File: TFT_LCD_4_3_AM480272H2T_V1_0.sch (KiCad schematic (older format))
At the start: 1 part, among them P1 HRS_FH28

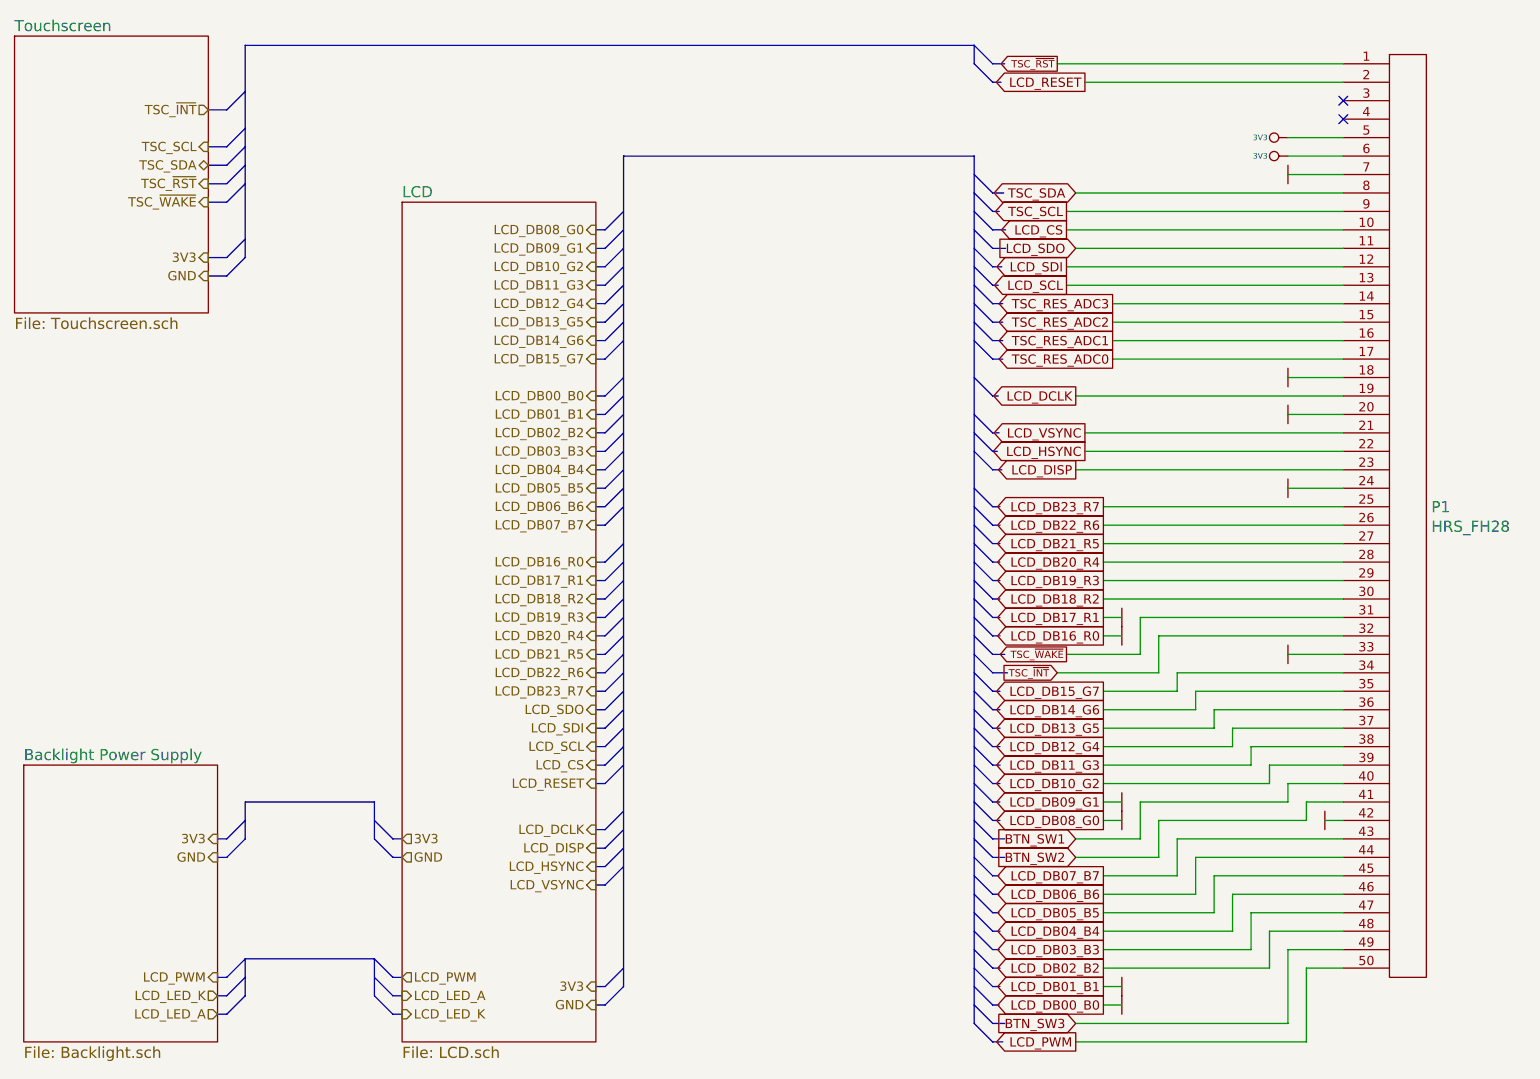
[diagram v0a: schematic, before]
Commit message: Schematic finished, needes to be rechecked, pcb finished needes to be tweeked
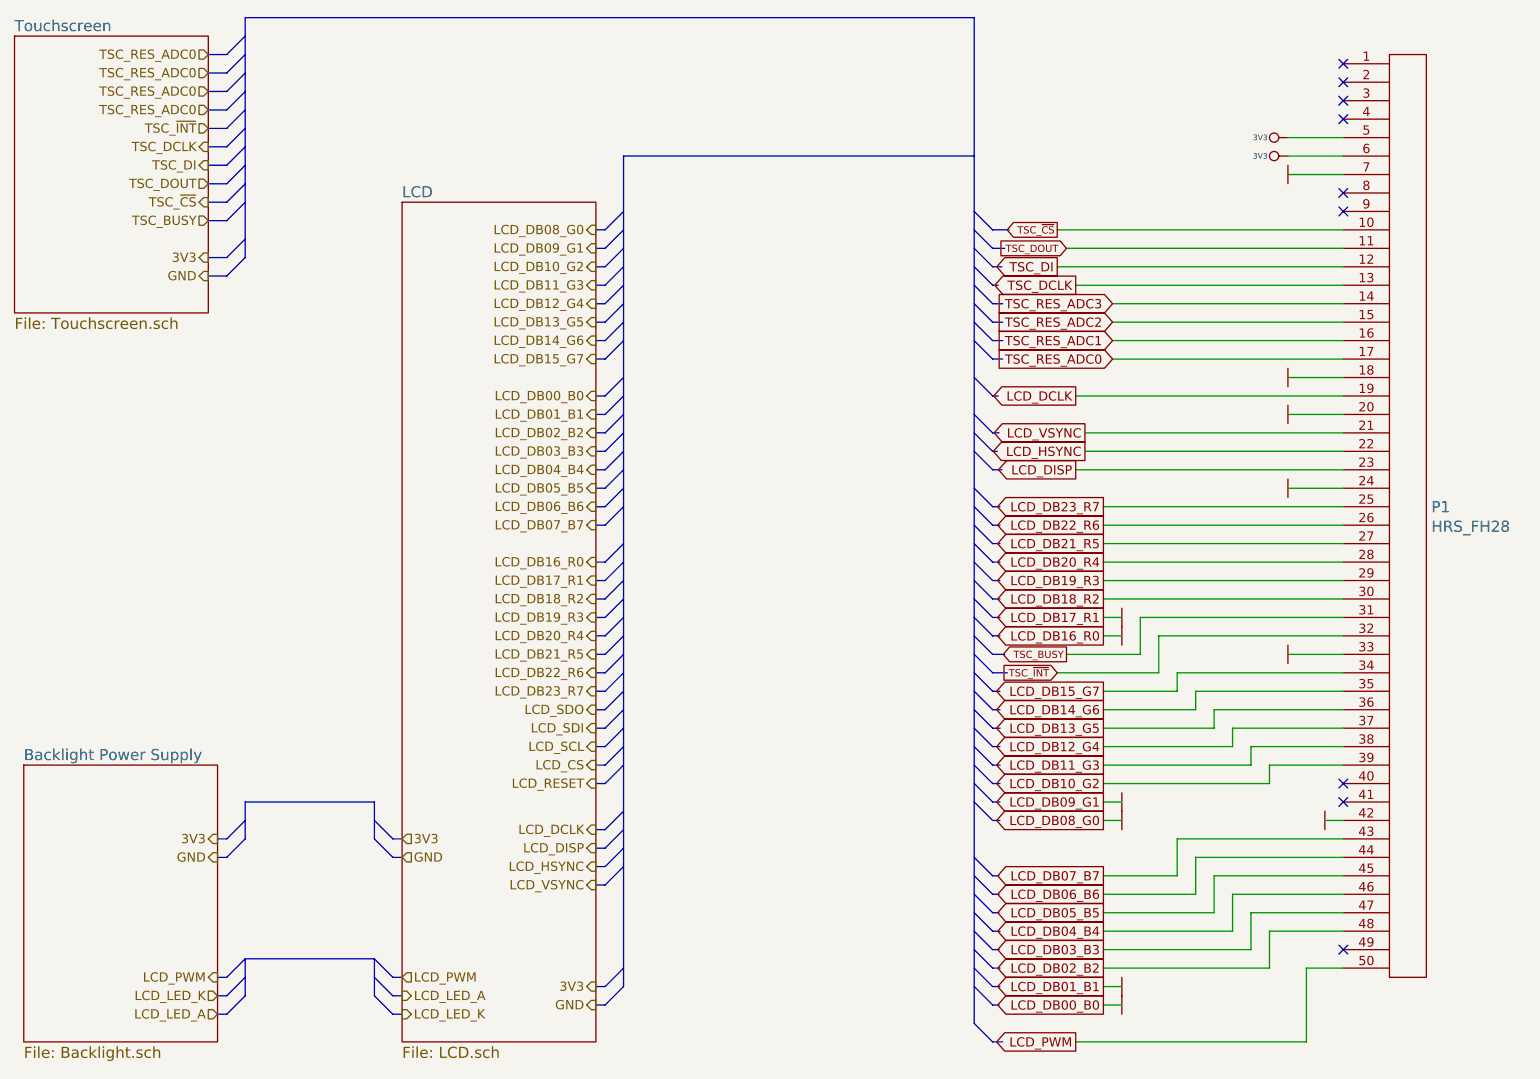
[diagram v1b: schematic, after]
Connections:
- net LCD_CS: no longer P1.10 (P10)
- net LCD_RESET: no longer P1.2 (P2)
- net LCD_SCL: no longer P1.13 (P3)
- net LCD_SDI: no longer P1.12 (P2)
- net LCD_SDO: no longer P1.11 (P1)
- net BTN_SW1: no longer names the net of P1.40 (P10)
- net BTN_SW2: no longer names the net of P1.41 (P1)
- net BTN_SW3: no longer names the net of P1.49 (P9)
- net TSC_SCL: no longer names the net of P1.9 (P9)
- net TSC_SDA: no longer names the net of P1.8 (P8)
- net TSC_~RST: no longer names the net of P1.1 (P1)
- net TSC_~WAKE renamed TSC_BUSY
- new net TSC_DCLK: P1.13 (P3)
- new net TSC_DI: P1.12 (P2)
- new net TSC_DOUT: P1.11 (P1)
- new net TSC_~CS: P1.10 (P10)
- no-connect marks 2 -> 9

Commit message: Corrected FPC 40pin top 0.5mm connector, generated again gerber and ps files
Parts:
- P1: symbol 50pin_HRS_FH28_Series_0_5mm -> Fpc_Connectors:50pin_HRS_FH28_Series_0_5mm
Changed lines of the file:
@@
-EESchema Schematic File Version 3
-LIBS:Capacitors_Smd0805
-LIBS:Capacitors_Smd_Tantal
-LIBS:Fpc_Connectors
-LIBS:Switching_Regulators
-LIBS:Diodes
-LIBS:Inductors
-LIBS:power
-LIBS:Resistors_Smd0603
-LIBS:Resistors_Smd0805
-LIBS:Symbols
-LIBS:Touch_Sensors
+EESchema Schematic File Version 4
 LIBS:TFT_LCD_4_3_AM480272H2T_V1_0-cache
 EELAYER 26 0
@@
 $EndSheet
 $Comp
-L GND #PWR01
+L power1:GND #PWR01
 U 1 1 57E98D5F
 P 9150 4950
@@
 $EndComp
 $Comp
-L 3V3 #PWR03
+L power1:3V3 #PWR03
 U 1 1 57E98DA1
 P 8950 1350
@@
 $EndComp
 $Comp
-L 3V3 #PWR04
+L power1:3V3 #PWR04
 U 1 1 57E98DD3
 P 8950 1250
@@
 LCD_DB15_G7
 $Comp
-L GND #PWR06
+L power1:GND #PWR06
 U 1 1 57E99A4F
 P 8050 5950
@@
 Text HLabel 5200 4250 0    50   Output ~ 0
 LCD_DB23_R7
-Text HLabel 5200 4450 0    50   Output ~ 0
-LCD_SDI
-Text HLabel 5200 4550 0    50   Output ~ 0
-LCD_SCL
-Text HLabel 5200 4650 0    50   Output ~ 0
-LCD_CS
-Text HLabel 5200 4750 0    50   Output ~ 0
-LCD_RESET
-$Sheet
-S 4150 1600 1050 4550
-U 578A9842
-F0 "LCD" 60
-F1 "LCD.sch" 60
-$EndSheet
 Text HLabel 5200 5000 0    50   Output ~ 0
 LCD_DCLK
@@
 TSC_DI
 $Comp
-L GND #PWR02
+L power1:GND #PWR02
 U 1 1 59E72514
 P 8050 5850
@@
 $EndComp
 $Comp
-L GND #PWR05
+L power1:GND #PWR05
 U 1 1 59E728D4
 P 8050 3950
@@
 $EndComp
 $Comp
-L GND #PWR07
+L power1:GND #PWR07
 U 1 1 59E728DA
 P 8050 3850
@@
 $EndComp
 $Comp
-L GND #PWR055
+L power1:GND #PWR055
 U 1 1 59E72AD4
 P 8050 4950
@@
 $EndComp
 $Comp
-L GND #PWR056
+L power1:GND #PWR056
 U 1 1 59E72ADA
 P 8050 4850
@@
 $EndComp
 $Comp
-L 50pin_HRS_FH28_Series_0_5mm P1
+L Fpc_Connectors:50pin_HRS_FH28_Series_0_5mm P1
 U 1 1 59E741FC
 P 9500 3250
@@
 $EndComp
 $Comp
-L GND #PWR057
+L power1:GND #PWR057
 U 1 1 59E7582B
 P 8950 4050
@@
 $EndComp
 $Comp
-L GND #PWR058
+L power1:GND #PWR058
 U 1 1 59E75840
 P 8950 3150
@@
 $EndComp
 $Comp
-L GND #PWR059
+L power1:GND #PWR059
 U 1 1 59E75858
 P 8950 2750
@@
 $EndComp
 $Comp
-L GND #PWR060
+L power1:GND #PWR060
 U 1 1 59E7586D
 P 8950 2550
@@
 $EndComp
 $Comp
-L GND #PWR061
+L power1:GND #PWR061
 U 1 1 59E75882
 P 8950 1450
@@
 Text GLabel 7750 1850 0    39   Input ~ 0
 TSC_DOUT
-Text HLabel 5200 4350 0    50   Output ~ 0
-LCD_SDO
 Entry Bus Bus
 	5250 4350 5350 4250
@@
 Wire Bus Line
 	3300 600  7250 600
+$Sheet
+S 4150 1600 1050 4550
+U 578A9842
+F0 "LCD" 60
+F1 "LCD.sch" 60
+$EndSheet
 $EndSCHEMATC
